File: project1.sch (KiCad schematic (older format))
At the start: 26 parts, among them P1 CONN_01X08, P2 CONN_01X02, P4 CONN_01X08, U1 LM7805CT, U2 LM741

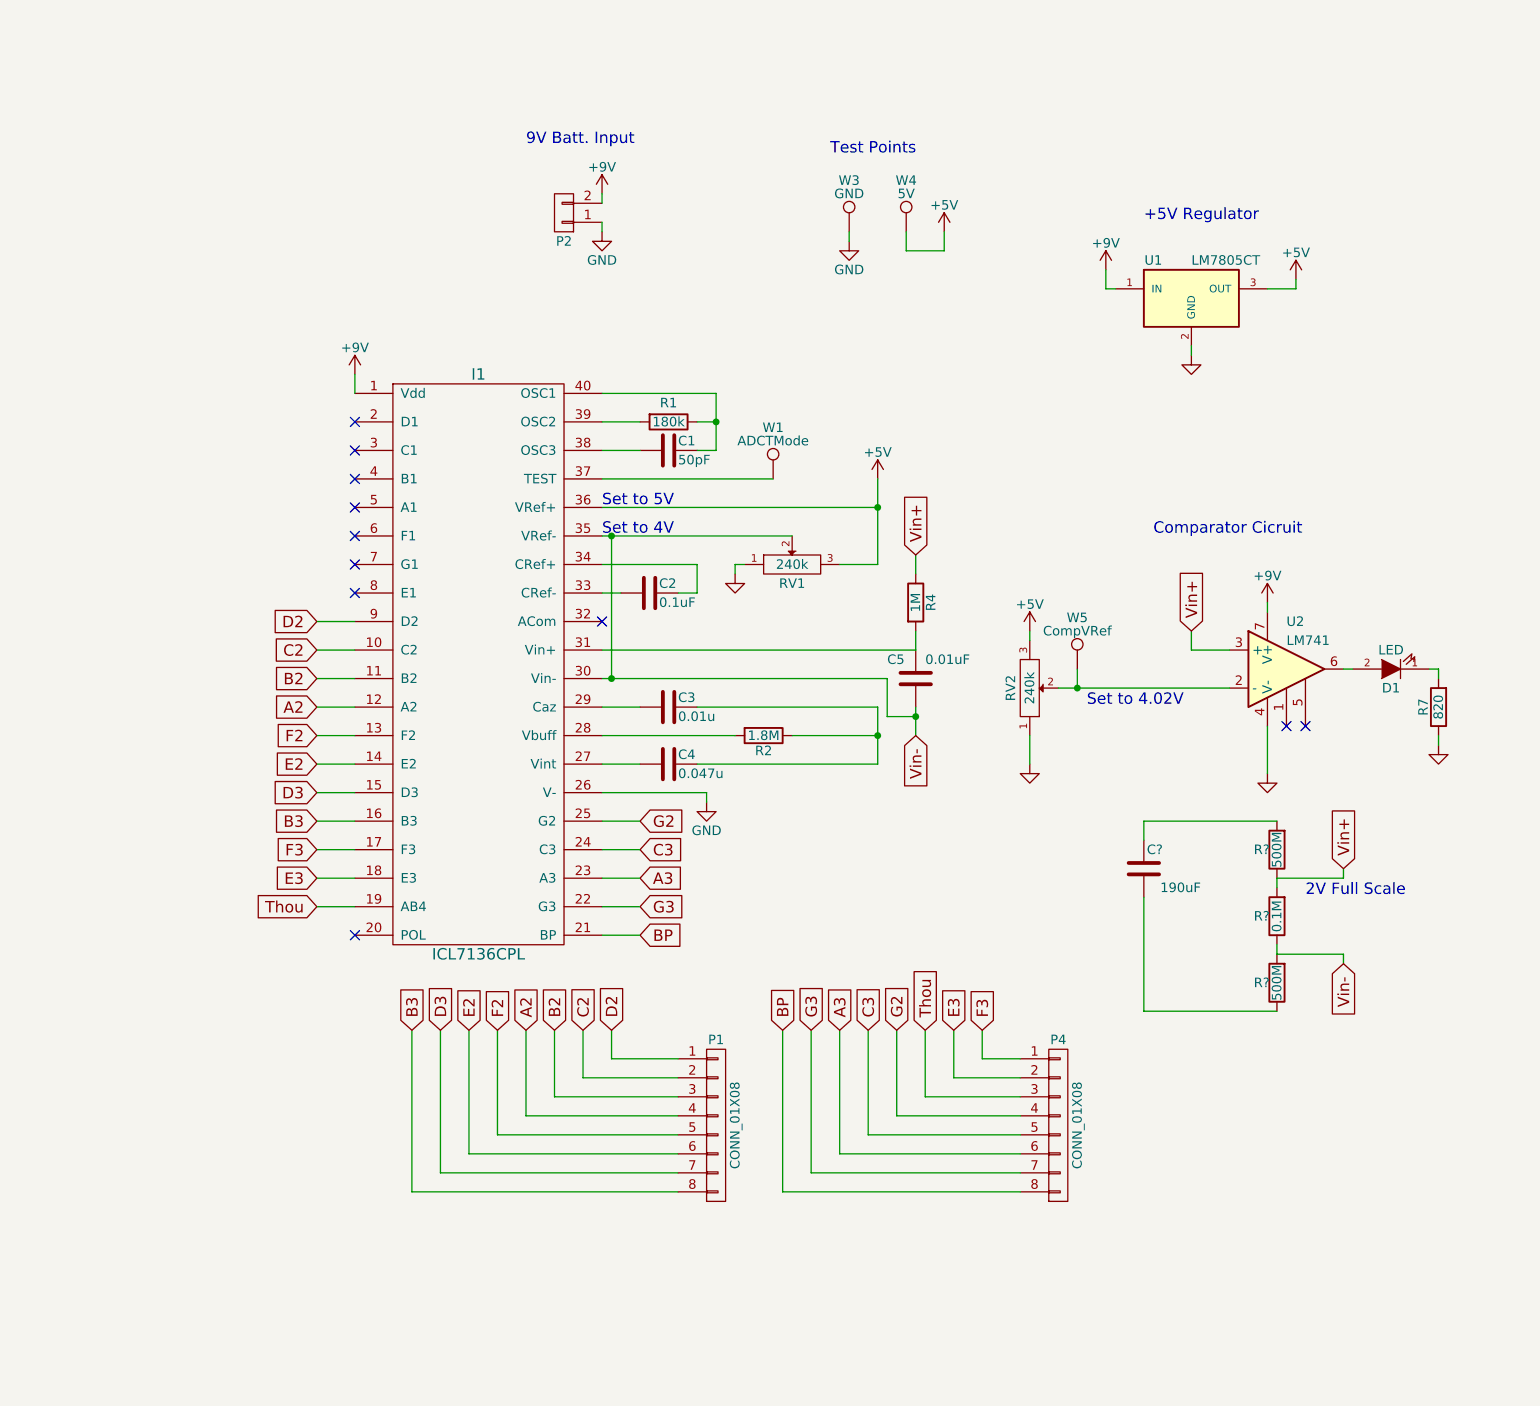
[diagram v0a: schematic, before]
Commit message: Updated Schematic Configuration; Needs Layout
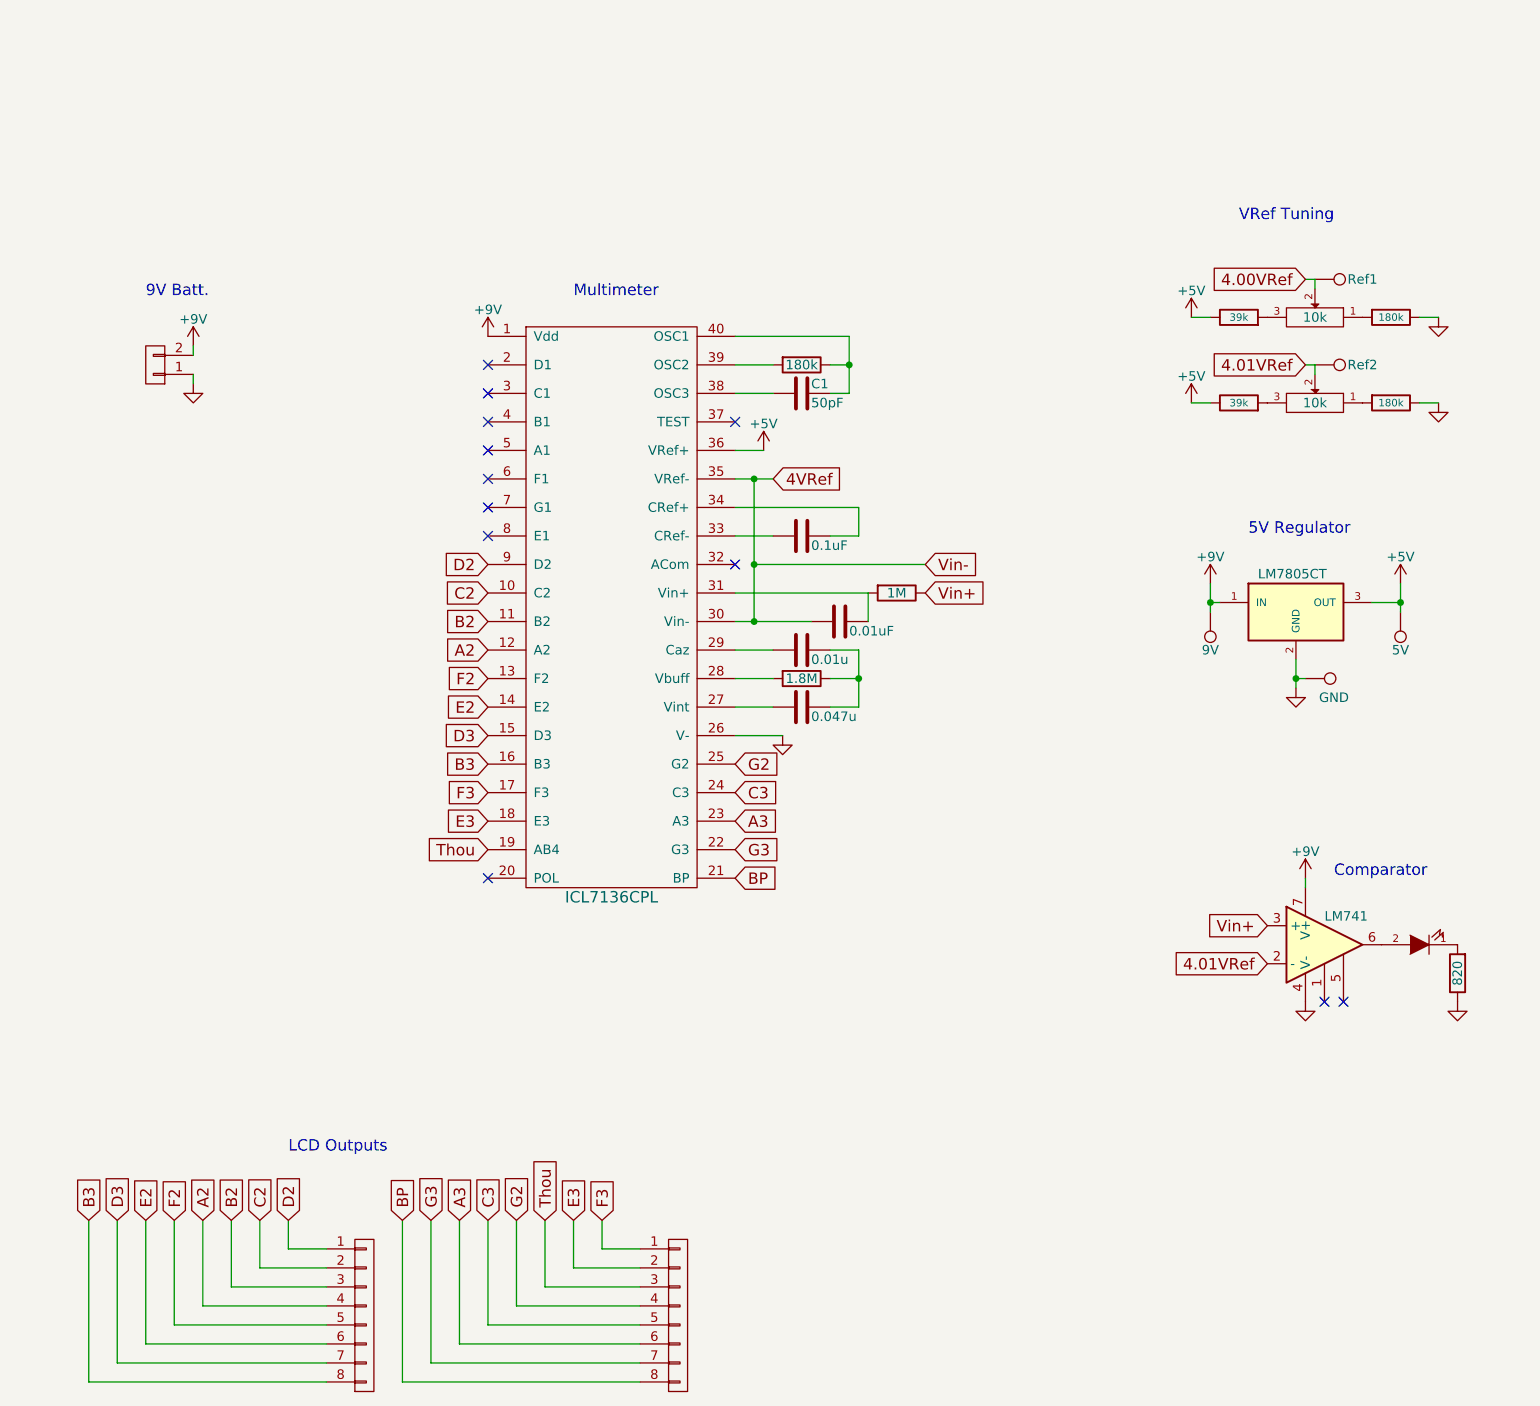
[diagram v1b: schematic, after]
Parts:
- removed C?: 190uF, Capacitors_ThroughHole:C_Rect_L7_W2.5_P5, symbol C
- removed R? (x2): 500M, Resistors_ThroughHole:Resistor_Horizontal_RM7mm, symbol R
- removed R?: 0.1M, Resistors_ThroughHole:Resistor_Horizontal_RM7mm, symbol R
- added R4, R6: 39k, Resistors_ThroughHole:Resistor_Horizontal_RM7mm, symbol R
- added R5, R7: 180k, Resistors_ThroughHole:Resistor_Horizontal_RM7mm, symbol R
- added W4: Ref1, Connect:PINTST, symbol TEST_1P
- RV1, RV2: value 240k -> 10k
- W1: value ADCTMode -> 9V
- W5: value CompVRef -> Ref2
- renumbered P2 to P1, P1 to P2, P4 to P3, R4 to R3, R7 to R8, W3 to W2, W4 to W3
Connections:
- net +5V: now also R4.1, R6.1; no longer RV1.3, RV2.3
- net +9V: now also W1.1
- net GND: now also R5.1, R7.1; no longer RV1.1, RV2.1
- net at I1.37 (TEST): no longer W1.1
- net 4.01VRef: now reaches RV2.2, U2.2 (-), W5.1
- net Vin- renamed 4VRef
- net 4VRef: no longer RV1.2
- new net: R7.2, RV2.1
- new net: R6.2, RV2.3
- new net: R5.2, RV1.1
- new net: R4.2, RV1.3
- new net 4.00VRef: RV1.2, W4.1
- no-connect marks 11 -> 12
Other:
- note added: "5V Regulator"
- note added: "9V Batt."
- note added: "Comparator"
- note added: "LCD Outputs"
- note added: "Multimeter"
- note added: "VRef Tuning"
- note removed: "+5V Regulator"
- note removed: "2V Full Scale"
- note removed: "9V Batt. Input"
- note removed: "Comparator Cicruit"
- note removed: "Set to 4.02V"
- note removed: "Set to 4V"
- note removed: "Set to 5V"
- note removed: "Test Points"
- moved on the sheet: C1

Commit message: full redesign
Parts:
- removed P2, P3: CONN_01X08, Pin_Headers:Pin_Header_Straight_1x08, symbol CONN_01X08
- removed U1: LM7805CT, TO_SOT_Packages_THT:TO-220_Neutral123_Horizontal, symbol LM7805CT
- removed U2: LM741, Housings_DIP:DIP-8_W7.62mm, symbol LM741
- added P10, P11, P12, P13, P14, P15, P16, P17, P18, P19, P20, P21, P22, P23, P24, P25, P26, P27, P28, P29, P7, P8, P9: CONN_02X01, IDC:Net_Tie_SMD, symbol CONN_02X01
- added P2, P5: CONN_01X04, Pin_Headers:Pin_Header_Straight_1x04, symbol CONN_01X04-RESCUE-project1
- added P3, P4, P6: CONN_02X04, IDC:IDC_Header_Straight_10pins, symbol CONN_02X04-RESCUE-project1
- added U1: LT1460GIZ-5, TO_SOT_Packages_THT:TO-92_Inline_Narrow_Oval, symbol LT1460GIZ-5
- added U2: TS912IN, Housings_DIP:DIP-8_W7.62mm, symbol TS912IN
- RV1, RV2: footprint Potentiometers:Potentiometer_Bourns_3339S_Angular_ScrewFront -> Potentiometers:Potentiometer_Bourns_3296W_3-8Zoll_Inline_ScrewUp
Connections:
- net labels added: A, A1, B, B1, C, C1, COM, D, D1, E, E1, F, F1, G, G1
- wire segments 74 -> 45
- no-connect marks 12 -> 6
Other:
- note added: "5V Reference"
- note added: "Display Outputs"
- note added: "Interconnects"
- note removed: "5V Regulator"
- note removed: "LCD Outputs"
- note removed: "Multimeter"
- moved on the sheet: C1

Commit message: latest revision
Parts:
- removed P2, P5: CONN_01X04, Pin_Headers:Pin_Header_Straight_1x04, symbol CONN_01X04-RESCUE-project1
- added LCD1: LCD-S101D40TR, IDC:LCD-S101D40TR, symbol LCD-S101D40TR
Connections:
- net labels removed: COM
- wire segments 45 -> 44
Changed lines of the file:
@@
 D2
 $Comp
-L GND #PWR5
+L GND #PWR01
 U 1 1 56C9353D
 P 4700 4650
-F 0 "#PWR5" H 4700 4400 50  0001 C CNN
+F 0 "#PWR01" H 4700 4400 50  0001 C CNN
 F 1 "GND" H 4700 4500 50  0001 C CNN
 F 2 "" H 4700 4650 50  0000 C CNN
@@
 NoConn ~ 3150 5400
 $Comp
-L +5V #PWR4
+L +5V #PWR02
 U 1 1 56C9FE61
 P 4600 3150
-F 0 "#PWR4" H 4600 3000 50  0001 C CNN
+F 0 "#PWR02" H 4600 3000 50  0001 C CNN
 F 1 "+5V" H 4600 3290 50  0000 C CNN
 F 2 "" H 4600 3150 50  0000 C CNN
@@
 $EndComp
 $Comp
-L +9V #PWR10
+L +9V #PWR03
 U 1 1 56CA283F
 P 6950 3750
-F 0 "#PWR10" H 6950 3600 50  0001 C CNN
+F 0 "#PWR03" H 6950 3600 50  0001 C CNN
 F 1 "+9V" H 6950 3890 50  0000 C CNN
 F 2 "" H 6950 3750 50  0000 C CNN
@@
 $EndComp
 $Comp
-L GND #PWR11
+L GND #PWR04
 U 1 1 56CA28BE
 P 7350 4000
-F 0 "#PWR11" H 7350 3750 50  0001 C CNN
+F 0 "#PWR04" H 7350 3750 50  0001 C CNN
 F 1 "GND" H 7350 3850 50  0001 C CNN
 F 2 "" H 7350 4000 50  0000 C CNN
@@
 $EndComp
 $Comp
-L +9V #PWR15
+L +9V #PWR05
 U 1 1 56CA3B6A
 P 8000 5000
-F 0 "#PWR15" H 8000 4850 50  0001 C CNN
+F 0 "#PWR05" H 8000 4850 50  0001 C CNN
 F 1 "+9V" H 8000 5140 50  0000 C CNN
 F 2 "" H 8000 5000 50  0000 C CNN
@@
 $EndComp
 $Comp
-L GND #PWR14
+L GND #PWR06
 U 1 1 56CA4DD8
 P 8000 1800
-F 0 "#PWR14" H 8000 1550 50  0001 C CNN
+F 0 "#PWR06" H 8000 1550 50  0001 C CNN
 F 1 "GND" H 8000 1650 50  0001 C CNN
 F 2 "" H 8000 1800 50  0000 C CNN
@@
 $EndComp
 $Comp
-L GND #PWR9
+L GND #PWR07
 U 1 1 56CA5077
 P 6850 5450
-F 0 "#PWR9" H 6850 5200 50  0001 C CNN
+F 0 "#PWR07" H 6850 5200 50  0001 C CNN
 F 1 "GND" H 6850 5300 50  0001 C CNN
 F 2 "" H 6850 5450 50  0000 C CNN
@@
 $EndComp
 $Comp
-L GND #PWR6
+L GND #PWR08
 U 1 1 56CA68D1
 P 6000 5300
-F 0 "#PWR6" H 6000 5050 50  0001 C CNN
+F 0 "#PWR08" H 6000 5050 50  0001 C CNN
 F 1 "GND" H 6000 5150 50  0001 C CNN
 F 2 "" H 6000 5300 50  0000 C CNN
@@
 $EndComp
 $Comp
-L +9V #PWR1
+L +9V #PWR09
 U 1 1 56CB8B59
 P 2450 1500
-F 0 "#PWR1" H 2450 1350 50  0001 C CNN
+F 0 "#PWR09" H 2450 1350 50  0001 C CNN
 F 1 "+9V" H 2450 1640 50  0000 C CNN
 F 2 "" H 2450 1500 50  0000 C CNN
@@
 $EndComp
 $Comp
-L GND #PWR2
+L GND #PWR010
 U 1 1 56CB8BA3
 P 2450 1700
-F 0 "#PWR2" H 2450 1450 50  0001 C CNN
+F 0 "#PWR010" H 2450 1450 50  0001 C CNN
 F 1 "GND" H 2450 1550 50  0001 C CNN
 F 2 "" H 2450 1700 50  0000 C CNN
@@
 NoConn ~ 4450 3750
 $Comp
-L +5V #PWR12
+L +5V #PWR011
 U 1 1 56E51696
 P 7750 3750
-F 0 "#PWR12" H 7750 3600 50  0001 C CNN
+F 0 "#PWR011" H 7750 3600 50  0001 C CNN
 F 1 "+5V" H 7750 3890 50  0000 C CNN
 F 2 "" H 7750 3750 50  0000 C CNN
@@
 Comparator
 $Comp
-L +5V #PWR8
+L +5V #PWR012
 U 1 1 56E53163
 P 6700 1800
-F 0 "#PWR8" H 6700 1650 50  0001 C CNN
+F 0 "#PWR012" H 6700 1650 50  0001 C CNN
 F 1 "+5V" H 6700 1940 50  0000 C CNN
 F 2 "" H 6700 1800 50  0000 C CNN
@@
 $EndComp
 $Comp
-L GND #PWR13
+L GND #PWR013
 U 1 1 56E74E6B
 P 8000 1350
-F 0 "#PWR13" H 8000 1100 50  0001 C CNN
+F 0 "#PWR013" H 8000 1100 50  0001 C CNN
 F 1 "GND" H 8000 1200 50  0001 C CNN
 F 2 "" H 8000 1350 50  0000 C CNN
@@
 $EndComp
 $Comp
-L +5V #PWR7
+L +5V #PWR014
 U 1 1 56E74E77
 P 6700 1350
-F 0 "#PWR7" H 6700 1200 50  0001 C CNN
+F 0 "#PWR014" H 6700 1200 50  0001 C CNN
 F 1 "+5V" H 6700 1490 50  0000 C CNN
 F 2 "" H 6700 1350 50  0000 C CNN
@@
 NoConn ~ 4450 3000
 $Comp
-L +9V #PWR3
+L +9V #PWR015
 U 1 1 56C9347C
 P 3150 2550
-F 0 "#PWR3" H 3150 2400 50  0001 C CNN
+F 0 "#PWR015" H 3150 2400 50  0001 C CNN
 F 1 "+9V" H 3150 2690 50  0000 C CNN
 F 2 "" H 3150 2550 50  0000 C CNN
@@
 Wire Wire Line
 	7750 3750 7750 3850
-Text GLabel 3650 1350 0    60   Input ~ 0
+Text GLabel 5050 1150 0    60   Input ~ 0
 BP
-$Comp
-L CONN_01X04-RESCUE-project1 P5
-U 1 1 57020C3E
-P 4550 1850
-F 0 "P5" H 4550 2100 50  0001 C CNN
-F 1 "CONN_01X04" V 4650 1850 50  0001 C CNN
-F 2 "Pin_Headers:Pin_Header_Straight_1x04" H 4550 1850 50  0001 C CNN
-F 3 "" H 4550 1850 50  0000 C CNN
-	1    4550 1850
-	0    1    1    0
-$EndComp
-Text GLabel 4800 1650 1    60   Input ~ 0
-COM
-Text GLabel 4650 1650 1    60   Input ~ 0
+Text GLabel 5050 1300 0    60   Input ~ 0
 E
-Text GLabel 4500 1650 1    60   Input ~ 0
+Text GLabel 5050 1450 0    60   Input ~ 0
 D
-Text GLabel 4350 1650 1    60   Input ~ 0
+Text GLabel 5050 1600 0    60   Input ~ 0
 C
-$Comp
-L CONN_01X04-RESCUE-project1 P2
-U 1 1 57021C28
-P 4600 950
-F 0 "P2" H 4600 1200 50  0001 C CNN
-F 1 "CONN_01X04" V 4700 950 50  0001 C CNN
-F 2 "Pin_Headers:Pin_Header_Straight_1x04" H 4600 950 50  0001 C CNN
-F 3 "" H 4600 950 50  0000 C CNN
-	1    4600 950
-	0    -1   -1   0
-$EndComp
-Text GLabel 4350 1150 3    60   Input ~ 0
+Text GLabel 5850 1600 2    60   Input ~ 0
 B
-Text GLabel 4500 1150 3    60   Input ~ 0
+Text GLabel 5850 1450 2    60   Input ~ 0
 A
-Text GLabel 4650 1150 3    60   Input ~ 0
+Text GLabel 5850 1300 2    60   Input ~ 0
 F
-Text GLabel 4800 1150 3    60   Input ~ 0
+Text GLabel 5850 1150 2    60   Input ~ 0
 G
-Text GLabel 3800 1350 2    60   Input ~ 0
-COM
 Text GLabel 2200 5150 2    60   Input ~ 0
 B
@@
 	1    0    0    -1
 $EndComp
-Text GLabel 1450 4200 2    60   Input ~ 0
+Text GLabel 1450 4350 2    60   Input ~ 0
 C3
-Text GLabel 1450 4350 2    60   Input ~ 0
+Text GLabel 1450 4650 2    60   Input ~ 0
 A3
-Text GLabel 1450 4500 2    60   Input ~ 0
+Text GLabel 950  4500 0    60   Input ~ 0
 G3
-Text GLabel 1450 4650 2    60   Input ~ 0
+Text GLabel 950  4650 0    60   Input ~ 0
 BP
 $Comp
@@
 BP
 Wire Wire Line
-	3650 1350 3800 1350
-Wire Wire Line
 	6400 5000 6850 5000
 NoConn ~ 7950 5150
@@
 Text GLabel 1450 3150 2    60   Input ~ 0
 A1
+Text GLabel 950  2850 0    60   Input ~ 0
+F1
 Text GLabel 950  3000 0    60   Input ~ 0
-F1
-Text GLabel 950  2850 0    60   Input ~ 0
 G1
 Text GLabel 950  2700 0    60   Input ~ 0
@@
 Text GLabel 1450 3450 2    60   Input ~ 0
 D2
+Text GLabel 950  3450 0    60   Input ~ 0
+E2
+Text GLabel 950  3750 0    60   Input ~ 0
+G2
 Text GLabel 950  3600 0    60   Input ~ 0
-E2
-Text GLabel 950  3450 0    60   Input ~ 0
-G2
-Text GLabel 950  3750 0    60   Input ~ 0
 F2
-Text GLabel 950  4650 0    60   Input ~ 0
+Text GLabel 950  4200 0    60   Input ~ 0
 E3
-Text GLabel 950  4500 0    60   Input ~ 0
+Text GLabel 950  4350 0    60   Input ~ 0
 F3
-Text GLabel 950  4350 0    60   Input ~ 0
+Text GLabel 1450 4500 2    60   Input ~ 0
 B3
-Text GLabel 950  4200 0    60   Input ~ 0
+Text GLabel 1450 4200 2    60   Input ~ 0
 D3
 $Comp
@@
 	1    0    0    -1
 $EndComp
+$Comp
+L LCD-S101D40TR LCD1
+U 1 1 570D6029
+P 5450 1400
+F 0 "LCD1" H 4900 2550 60  0001 C CNN
+F 1 "LCD-S101D40TR" H 5450 1800 39  0000 C CNN
+F 2 "IDC:LCD-S101D40TR" V 5250 1500 60  0001 C CNN
+F 3 "" V 5250 1500 60  0000 C CNN
+	1    5450 1400
+	1    0    0    -1
+$EndComp
